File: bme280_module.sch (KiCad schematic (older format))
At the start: 2 parts, among them U1 bme280

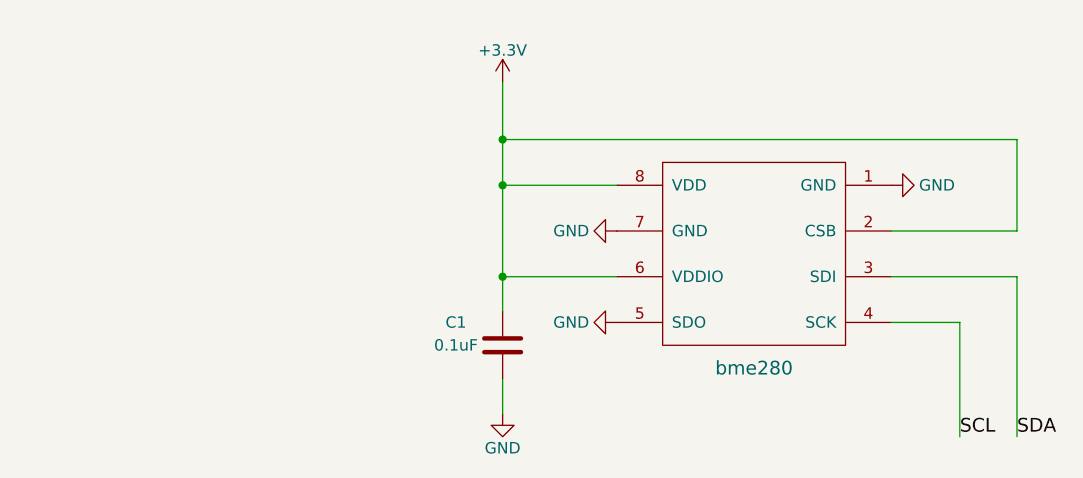
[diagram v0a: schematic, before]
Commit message: Add netlist and pcb design
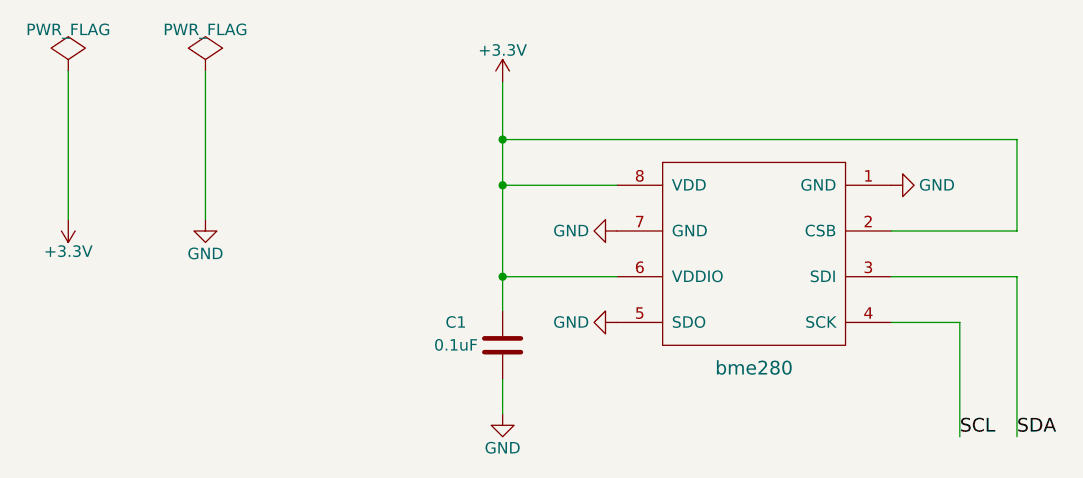
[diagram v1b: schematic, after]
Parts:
- C1: footprint (none) -> Capacitors_SMD:C_0603
- U1: footprint (none) -> bme280:bme280
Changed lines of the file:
@@
 LIBS:valves
 LIBS:bme280
+LIBS:bme280_module-cache
 EELAYER 25 0
 EELAYER END
@@
 F 0 "U1" H 5350 3250 60  0001 C CNN
 F 1 "bme280" H 5700 3250 60  0000 C CNN
-F 2 "" H 5700 3750 60  0001 C CNN
+F 2 "bme280:bme280" H 5700 3750 60  0001 C CNN
 F 3 "" H 5700 3750 60  0001 C CNN
 	1    5700 3750
@@
 $EndComp
 $Comp
-L GND #PWR?
-U 1 1 58D2795E
-P 4600 4450
-F 0 "#PWR?" H 4600 4200 50  0001 C CNN
-F 1 "GND" H 4600 4300 50  0000 C CNN
-F 2 "" H 4600 4450 50  0000 C CNN
-F 3 "" H 4600 4450 50  0000 C CNN
-	1    4600 4450
-	1    0    0    -1
-$EndComp
-$Comp
-L +3.3V #PWR?
+L +3.3V #PWR01
 U 1 1 58D27988
 P 4600 3000
-F 0 "#PWR?" H 4600 2850 50  0001 C CNN
+F 0 "#PWR01" H 4600 2850 50  0001 C CNN
 F 1 "+3.3V" H 4600 3140 50  0000 C CNN
 F 2 "" H 4600 3000 50  0000 C CNN
@@
 F 0 "C1" H 4350 4250 50  0000 L CNN
 F 1 "0.1uF" H 4300 4150 50  0000 L CNN
-F 2 "" H 4638 4000 50  0000 C CNN
+F 2 "Capacitors_SMD:C_0603" H 4638 4000 50  0001 C CNN
 F 3 "" H 4600 4150 50  0000 C CNN
 	1    4600 4150
 	1    0    0    -1
-$EndComp
-$Comp
-L GND #PWR?
-U 1 1 58D27D49
-P 5100 3650
-F 0 "#PWR?" H 5100 3400 50  0001 C CNN
-F 1 "GND" V 5100 3450 50  0000 C CNN
-F 2 "" H 5100 3650 50  0000 C CNN
-F 3 "" H 5100 3650 50  0000 C CNN
-	1    5100 3650
-	0    1    1    0
-$EndComp
-$Comp
-L GND #PWR?
-U 1 1 58D27D7B
-P 6300 3450
-F 0 "#PWR?" H 6300 3200 50  0001 C CNN
-F 1 "GND" V 6300 3250 50  0000 C CNN
-F 2 "" H 6300 3450 50  0000 C CNN
-F 3 "" H 6300 3450 50  0000 C CNN
-	1    6300 3450
-	0    -1   -1   0
 $EndComp
 Wire Wire Line
@@
 	6300 3650 6850 3650
 Wire Wire Line
-	6850 3250 6850 3650
+	6850 3650 6850 3250
 Wire Wire Line
-	4600 3250 6850 3250
+	6850 3250 4600 3250
 Connection ~ 4600 3250
 Connection ~ 4600 3850
@@
 SDA
 $Comp
-L GND #PWR?
-U 1 1 58D27ECD
+L PWR_FLAG #FLG02
+U 1 1 58D28284
+P 2700 2950
+F 0 "#FLG02" H 2700 3045 50  0001 C CNN
+F 1 "PWR_FLAG" H 2700 3130 50  0000 C CNN
+F 2 "" H 2700 2950 50  0000 C CNN
+F 3 "" H 2700 2950 50  0000 C CNN
+	1    2700 2950
+	1    0    0    -1
+$EndComp
+$Comp
+L PWR_FLAG #FLG03
+U 1 1 58D28299
+P 3300 2950
+F 0 "#FLG03" H 3300 3045 50  0001 C CNN
+F 1 "PWR_FLAG" H 3300 3130 50  0000 C CNN
+F 2 "" H 3300 2950 50  0000 C CNN
+F 3 "" H 3300 2950 50  0000 C CNN
+	1    3300 2950
+	1    0    0    -1
+$EndComp
+$Comp
+L +3.3V #PWR04
+U 1 1 58D282A9
+P 2700 3600
+F 0 "#PWR04" H 2700 3450 50  0001 C CNN
+F 1 "+3.3V" H 2700 3740 50  0000 C CNN
+F 2 "" H 2700 3600 50  0000 C CNN
+F 3 "" H 2700 3600 50  0000 C CNN
+	1    2700 3600
+	-1   0    0    1
+$EndComp
+$Comp
+L GND #PWR05
+U 1 1 58D282C0
+P 3300 3600
+F 0 "#PWR05" H 3300 3350 50  0001 C CNN
+F 1 "GND" H 3300 3450 50  0000 C CNN
+F 2 "" H 3300 3600 50  0000 C CNN
+F 3 "" H 3300 3600 50  0000 C CNN
+	1    3300 3600
+	1    0    0    -1
+$EndComp
+Wire Wire Line
+	2700 2950 2700 3600
+Wire Wire Line
+	3300 2950 3300 3600
+$Comp
+L GND #PWR06
+U 1 1 58D284B6
+P 4600 4450
+F 0 "#PWR06" H 4600 4200 50  0001 C CNN
+F 1 "GND" H 4600 4300 50  0000 C CNN
+F 2 "" H 4600 4450 50  0000 C CNN
+F 3 "" H 4600 4450 50  0000 C CNN
+	1    4600 4450
+	1    0    0    -1
+$EndComp
+$Comp
+L GND #PWR07
+U 1 1 58D284CD
+P 5100 3650
+F 0 "#PWR07" H 5100 3400 50  0001 C CNN
+F 1 "GND" V 5100 3450 50  0000 C CNN
+F 2 "" H 5100 3650 50  0000 C CNN
+F 3 "" H 5100 3650 50  0000 C CNN
+	1    5100 3650
+	0    1    1    0
+$EndComp
+$Comp
+L GND #PWR08
+U 1 1 58D284DB
+P 6300 3450
+F 0 "#PWR08" H 6300 3200 50  0001 C CNN
+F 1 "GND" V 6300 3250 50  0000 C CNN
+F 2 "" H 6300 3450 50  0000 C CNN
+F 3 "" H 6300 3450 50  0000 C CNN
+	1    6300 3450
+	0    -1   -1   0
+$EndComp
+$Comp
+L GND #PWR09
+U 1 1 58D2855B
 P 5100 4050
-F 0 "#PWR?" H 5100 3800 50  0001 C CNN
+F 0 "#PWR09" H 5100 3800 50  0001 C CNN
 F 1 "GND" V 5100 3850 50  0000 C CNN
 F 2 "" H 5100 4050 50  0000 C CNN
